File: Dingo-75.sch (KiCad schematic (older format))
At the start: 178 parts, among them SW1 SW_Push, U1 AT90USB1286-AU, Y1 16MHz

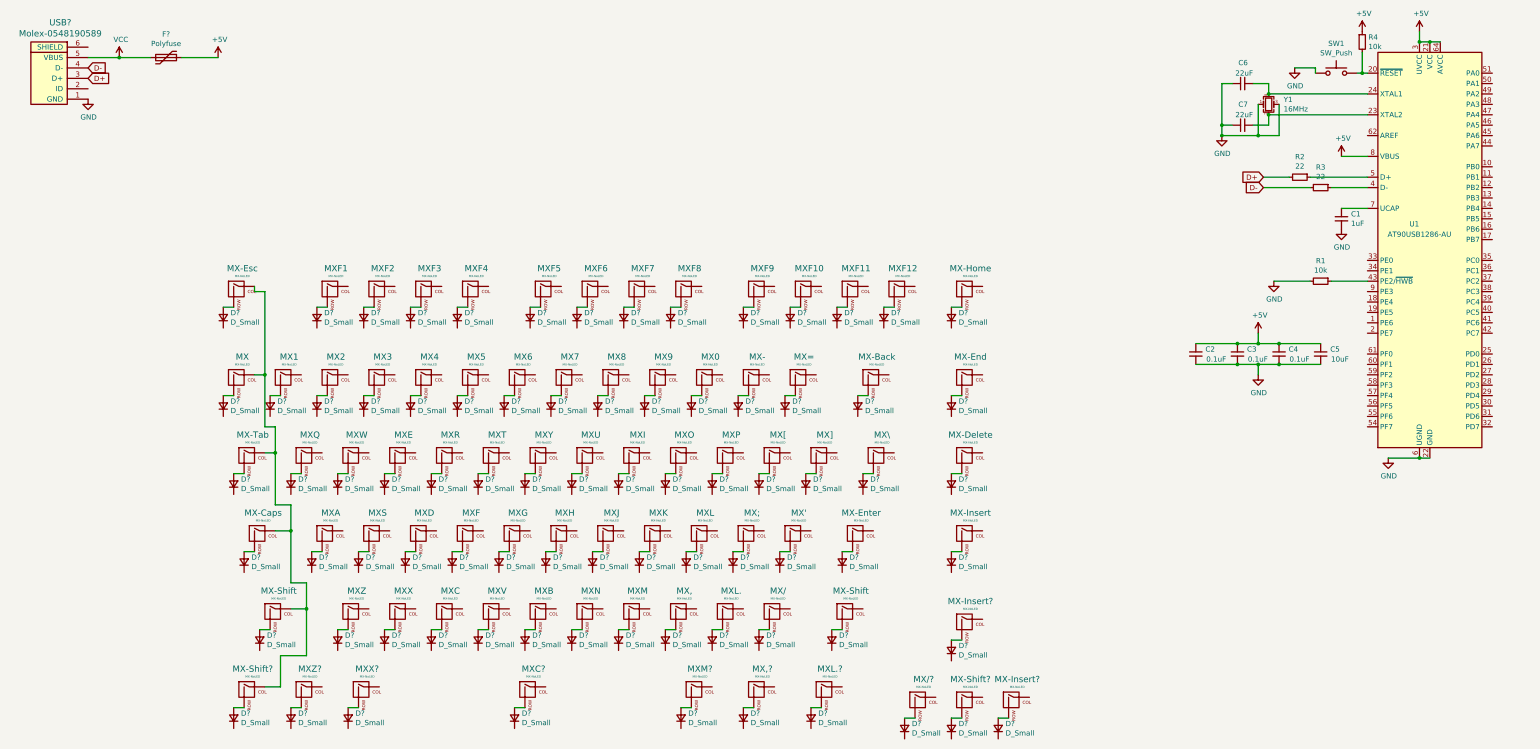
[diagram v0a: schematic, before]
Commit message: Completed switch matrix, started footprint assignment
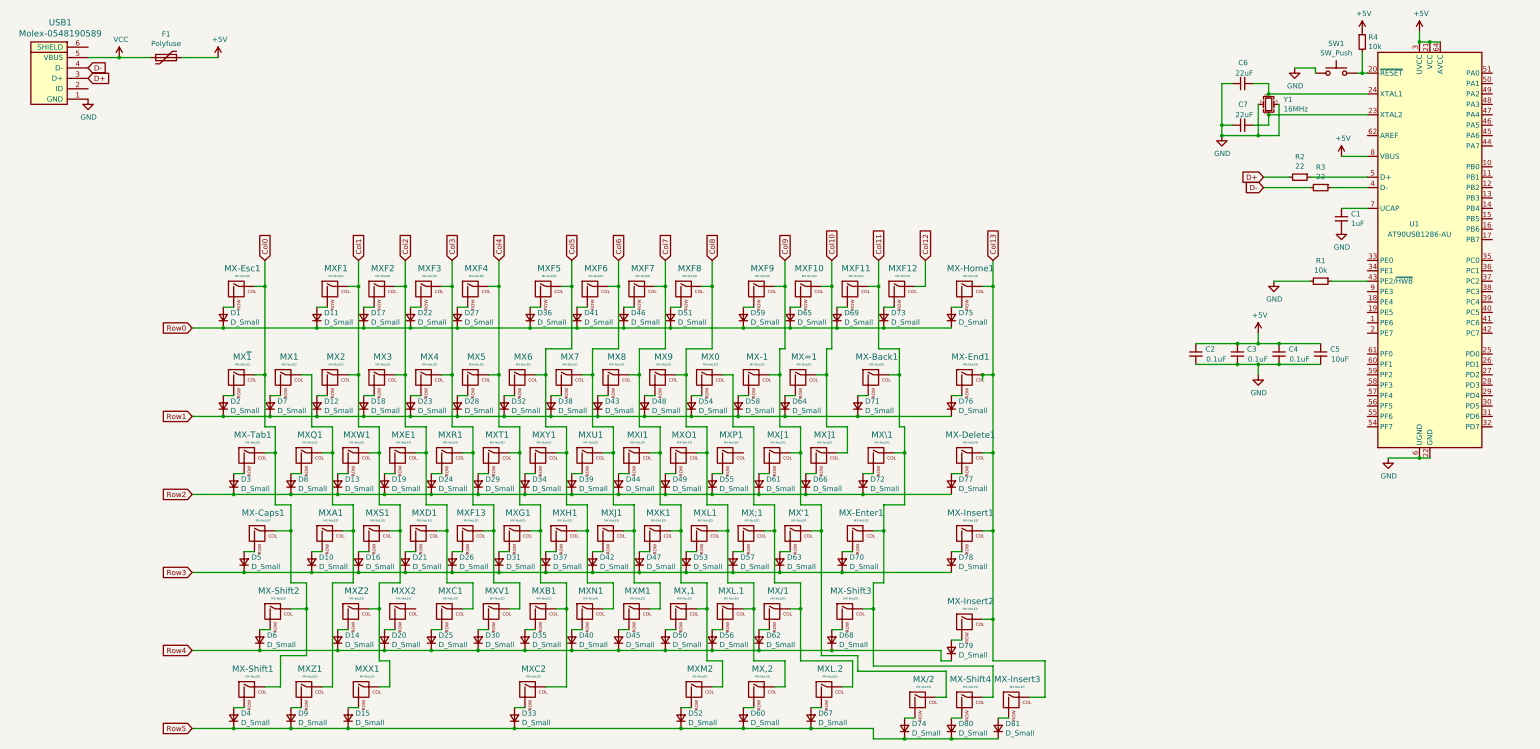
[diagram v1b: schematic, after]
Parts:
- C1, C2, C3, C4, C5, C6, C7: footprint (none) -> Capacitor_SMD:C_0805_2012Metric
- D1, D10, D11, D12, D13, D14, D15, D16, D17, D18, D19, D2, D20, D21, D22, D23, D24, D25, D26, D27, D28, D29, D3, D30, D31, D32, D33, D34, D35, D36, D37, D38, D39, D4, D40, D41, D42, D43, D44, D45, D46, D47, D48, D49, D5, D50, D51, D52, D53, D54, D55, D56, D57, D58, D59, D6, D60, D61, D62, D63, D64, D65, D66, D67, D68, D69, D7, D70, D71, D72, D73, D74, D75, D76, D77, D78, D79, D8, D80, D81, D9: renamed from D?; footprint (none) -> Diode_SMD:D_SOD-123
- F1: renamed from F?; footprint (none) -> Fuse:Fuse_1206_3216Metric
- MX'1: renamed from MX'; footprint (none) -> MX_Alps_Hybrid:MX-1U-NoLED
- MX,1: renamed from MX,; footprint (none) -> MX_Alps_Hybrid:MX-1U-NoLED
- MX,2: renamed from MX,?; footprint (none) -> MX_Alps_Hybrid:MX-1U-NoLED
- MX-1: renamed from MX-; footprint (none) -> MX_Alps_Hybrid:MX-1U-NoLED
- MX-Back1: renamed from MX-Back; footprint (none) -> MX_Alps_Hybrid:MX-1U-NoLED
- MX-Caps1: renamed from MX-Caps; footprint (none) -> MX_Alps_Hybrid:MX-1U-NoLED
- MX-Delete1: renamed from MX-Delete; footprint (none) -> MX_Alps_Hybrid:MX-1U-NoLED
- MX-End1: renamed from MX-End; footprint (none) -> MX_Alps_Hybrid:MX-1U-NoLED
- MX-Enter1: renamed from MX-Enter; footprint (none) -> MX_Alps_Hybrid:MX-1U-NoLED
- MX-Esc1: renamed from MX-Esc; footprint (none) -> MX_Alps_Hybrid:MX-1U-NoLED
- MX-Home1: renamed from MX-Home; footprint (none) -> MX_Alps_Hybrid:MX-1U-NoLED
- MX-Insert1: renamed from MX-Insert; footprint (none) -> MX_Alps_Hybrid:MX-1U-NoLED
- MX-Insert2, MX-Insert3: renamed from MX-Insert?; footprint (none) -> MX_Alps_Hybrid:MX-1U-NoLED
- MX-Shift1, MX-Shift4: renamed from MX-Shift?; footprint (none) -> MX_Alps_Hybrid:MX-1U-NoLED
- MX-Shift2, MX-Shift3: renamed from MX-Shift; footprint (none) -> MX_Alps_Hybrid:MX-1U-NoLED
- MX-Tab1: renamed from MX-Tab; footprint (none) -> MX_Alps_Hybrid:MX-1U-NoLED
- MX/1: renamed from MX/; footprint (none) -> MX_Alps_Hybrid:MX-1U-NoLED
- MX/2: renamed from MX/?; footprint (none) -> MX_Alps_Hybrid:MX-1U-NoLED
- MX0, MX1, MX2, MX3, MX4, MX5, MX6, MX7, MX8, MX9, MXF1, MXF10, MXF11, MXF12, MXF2, MXF3, MXF4, MXF5, MXF6, MXF7, MXF8, MXF9: footprint (none) -> MX_Alps_Hybrid:MX-1U-NoLED
- MX;1: renamed from MX;; footprint (none) -> MX_Alps_Hybrid:MX-1U-NoLED
- MX=1: renamed from MX=; footprint (none) -> MX_Alps_Hybrid:MX-1U-NoLED
- MXA1: renamed from MXA; footprint (none) -> MX_Alps_Hybrid:MX-1U-NoLED
- MXB1: renamed from MXB; footprint (none) -> MX_Alps_Hybrid:MX-1U-NoLED
- MXC1: renamed from MXC; footprint (none) -> MX_Alps_Hybrid:MX-1U-NoLED
- MXC2: renamed from MXC?; footprint (none) -> MX_Alps_Hybrid:MX-1U-NoLED
- MXD1: renamed from MXD; footprint (none) -> MX_Alps_Hybrid:MX-1U-NoLED
- MXE1: renamed from MXE; footprint (none) -> MX_Alps_Hybrid:MX-1U-NoLED
- MXF13: renamed from MXF; footprint (none) -> MX_Alps_Hybrid:MX-1U-NoLED
- MXG1: renamed from MXG; footprint (none) -> MX_Alps_Hybrid:MX-1U-NoLED
- MXH1: renamed from MXH; footprint (none) -> MX_Alps_Hybrid:MX-1U-NoLED
- MXI1: renamed from MXI; footprint (none) -> MX_Alps_Hybrid:MX-1U-NoLED
- MXJ1: renamed from MXJ; footprint (none) -> MX_Alps_Hybrid:MX-1U-NoLED
- MXK1: renamed from MXK; footprint (none) -> MX_Alps_Hybrid:MX-1U-NoLED
- MXL.1: renamed from MXL.; footprint (none) -> MX_Alps_Hybrid:MX-1U-NoLED
- MXL.2: renamed from MXL.?; footprint (none) -> MX_Alps_Hybrid:MX-1U-NoLED
- MXL1: renamed from MXL; footprint (none) -> MX_Alps_Hybrid:MX-1U-NoLED
- MXM1: renamed from MXM; footprint (none) -> MX_Alps_Hybrid:MX-1U-NoLED
- MXM2: renamed from MXM?; footprint (none) -> MX_Alps_Hybrid:MX-1U-NoLED
- MXN1: renamed from MXN; footprint (none) -> MX_Alps_Hybrid:MX-1U-NoLED
- MXO1: renamed from MXO; footprint (none) -> MX_Alps_Hybrid:MX-1U-NoLED
- MXP1: renamed from MXP; footprint (none) -> MX_Alps_Hybrid:MX-1U-NoLED
- MXQ1: renamed from MXQ; footprint (none) -> MX_Alps_Hybrid:MX-1U-NoLED
- MXR1: renamed from MXR; footprint (none) -> MX_Alps_Hybrid:MX-1U-NoLED
- MXS1: renamed from MXS; footprint (none) -> MX_Alps_Hybrid:MX-1U-NoLED
- MXT1: renamed from MXT; footprint (none) -> MX_Alps_Hybrid:MX-1U-NoLED
- MXU1: renamed from MXU; footprint (none) -> MX_Alps_Hybrid:MX-1U-NoLED
- MXV1: renamed from MXV; footprint (none) -> MX_Alps_Hybrid:MX-1U-NoLED
- MXW1: renamed from MXW; footprint (none) -> MX_Alps_Hybrid:MX-1U-NoLED
- MXX1: renamed from MXX?; footprint (none) -> MX_Alps_Hybrid:MX-1U-NoLED
- MXX2: renamed from MXX; footprint (none) -> MX_Alps_Hybrid:MX-1U-NoLED
- MXY1: renamed from MXY; footprint (none) -> MX_Alps_Hybrid:MX-1U-NoLED
- MXZ1: renamed from MXZ?; footprint (none) -> MX_Alps_Hybrid:MX-1U-NoLED
- MXZ2: renamed from MXZ; footprint (none) -> MX_Alps_Hybrid:MX-1U-NoLED
- MX[1: renamed from MX[; footprint (none) -> MX_Alps_Hybrid:MX-1U-NoLED
- MX\1: renamed from MX\; footprint (none) -> MX_Alps_Hybrid:MX-1U-NoLED
- MX]1: renamed from MX]; footprint (none) -> MX_Alps_Hybrid:MX-1U-NoLED
- MX~1: renamed from MX~; footprint (none) -> MX_Alps_Hybrid:MX-1U-NoLED
- R1, R2, R3, R4: footprint (none) -> Resistor_SMD:R_0805_2012Metric
- gave numbers to parts that had none: 1
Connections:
- net Col0: now reaches MX-Caps1.1 (COL), MX-Esc1.1 (COL), MX-Shift1.1 (COL), MX-Shift2.1 (COL), MX-Tab1.1 (COL), MX~1.1 (COL)
- net Row1: now reaches D2.1 (K)
- net Row1: now also D12.1 (K), D18.1 (K), D23.1 (K), D28.1 (K), D32.1 (K), D38.1 (K), D43.1 (K), D48.1 (K), D54.1 (K), D58.1 (K), D64.1 (K), D7.1 (K), D71.1 (K), D76.1 (K)
- net at MX1.1 (COL): now also MXA1.1 (COL), MXQ1.1 (COL), MXZ1.1 (COL)
- net Col1: now reaches MX2.1 (COL)
- net Col1: now also MXF1.1 (COL), MXS1.1 (COL), MXW1.1 (COL), MXX1.1 (COL), MXZ2.1 (COL)
- net Col2: now reaches MX3.1 (COL)
- net Col2: now also MXC1.1 (COL), MXD1.1 (COL), MXE1.1 (COL), MXF2.1 (COL)
- net Col3: now reaches MX4.1 (COL)
- net Col3: now also MXF13.1 (COL), MXF3.1 (COL), MXR1.1 (COL), MXV1.1 (COL)
- net Col4: now reaches MX5.1 (COL)
- net Col4: now also MXB1.1 (COL), MXC2.1 (COL), MXF4.1 (COL), MXG1.1 (COL), MXT1.1 (COL)
- net Col5: now reaches MX6.1 (COL)
- net Col5: now also MXF5.1 (COL), MXH1.1 (COL), MXN1.1 (COL), MXY1.1 (COL)
- net Col6: now reaches MX7.1 (COL)
- net Col6: now also MXF6.1 (COL), MXJ1.1 (COL), MXM1.1 (COL), MXU1.1 (COL)
- net Col7: now reaches MX8.1 (COL)
- net Col7: now also MX,1.1 (COL), MXF7.1 (COL), MXI1.1 (COL), MXK1.1 (COL), MXM2.1 (COL)
- net Col8: now reaches MX9.1 (COL)
- net Col8: now also MX,2.1 (COL), MXF8.1 (COL), MXL.1.1 (COL), MXL1.1 (COL), MXO1.1 (COL)
- net at MX0.1 (COL): now also MX/1.1 (COL), MX;1.1 (COL), MXL.2.1 (COL)
- net Col9: now reaches MX-1.1 (COL)
- net Col9: now also MX'1.1 (COL), MX/2.1 (COL), MXF9.1 (COL), MX[1.1 (COL)
- net Col10: now reaches MX=1.1 (COL)
- net Col10: now also MXF10.1 (COL), MX]1.1 (COL)
- net Col11: now reaches MX-Back1.1 (COL)
- net Col11: now also MX-Enter1.1 (COL), MX-Shift3.1 (COL), MX-Shift4.1 (COL), MXF11.1 (COL), MX\1.1 (COL)
- net Col13: now reaches MX-End1.1 (COL)
- net Col13: now also MX-Delete1.1 (COL), MX-Home1.1 (COL), MX-Insert1.1 (COL), MX-Insert2.1 (COL), MX-Insert3.1 (COL)
- net Row0: now reaches D1.1 (K)
- net Row0: now also D11.1 (K), D17.1 (K), D22.1 (K), D27.1 (K), D36.1 (K), D41.1 (K), D46.1 (K), D51.1 (K), D59.1 (K), D65.1 (K), D69.1 (K), D73.1 (K), D75.1 (K)
- net Col12: now reaches MXF12.1 (COL)
- net Row2: now reaches D3.1 (K)
- net Row2: now also D13.1 (K), D19.1 (K), D24.1 (K), D29.1 (K), D34.1 (K), D39.1 (K), D44.1 (K), D49.1 (K), D55.1 (K), D61.1 (K), D66.1 (K), D72.1 (K), D77.1 (K), D8.1 (K)
- net Row3: now reaches D5.1 (K)
- net Row3: now also D10.1 (K), D16.1 (K), D21.1 (K), D26.1 (K), D31.1 (K), D37.1 (K), D42.1 (K), D47.1 (K), D53.1 (K), D57.1 (K), D63.1 (K), D70.1 (K), D78.1 (K)
- net Row4: now reaches D6.1 (K)
- net Row4: now also D14.1 (K), D20.1 (K), D25.1 (K), D30.1 (K), D35.1 (K), D40.1 (K), D45.1 (K), D50.1 (K), D56.1 (K), D62.1 (K), D68.1 (K), D79.1 (K)
- net Row5: now reaches D4.1 (K)
- net Row5: now also D15.1 (K), D33.1 (K), D52.1 (K), D60.1 (K), D67.1 (K), D74.1 (K), D80.1 (K), D81.1 (K), D9.1 (K)

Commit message: Completed Footprint Assignment, Completed Board Layout, Started trace routing
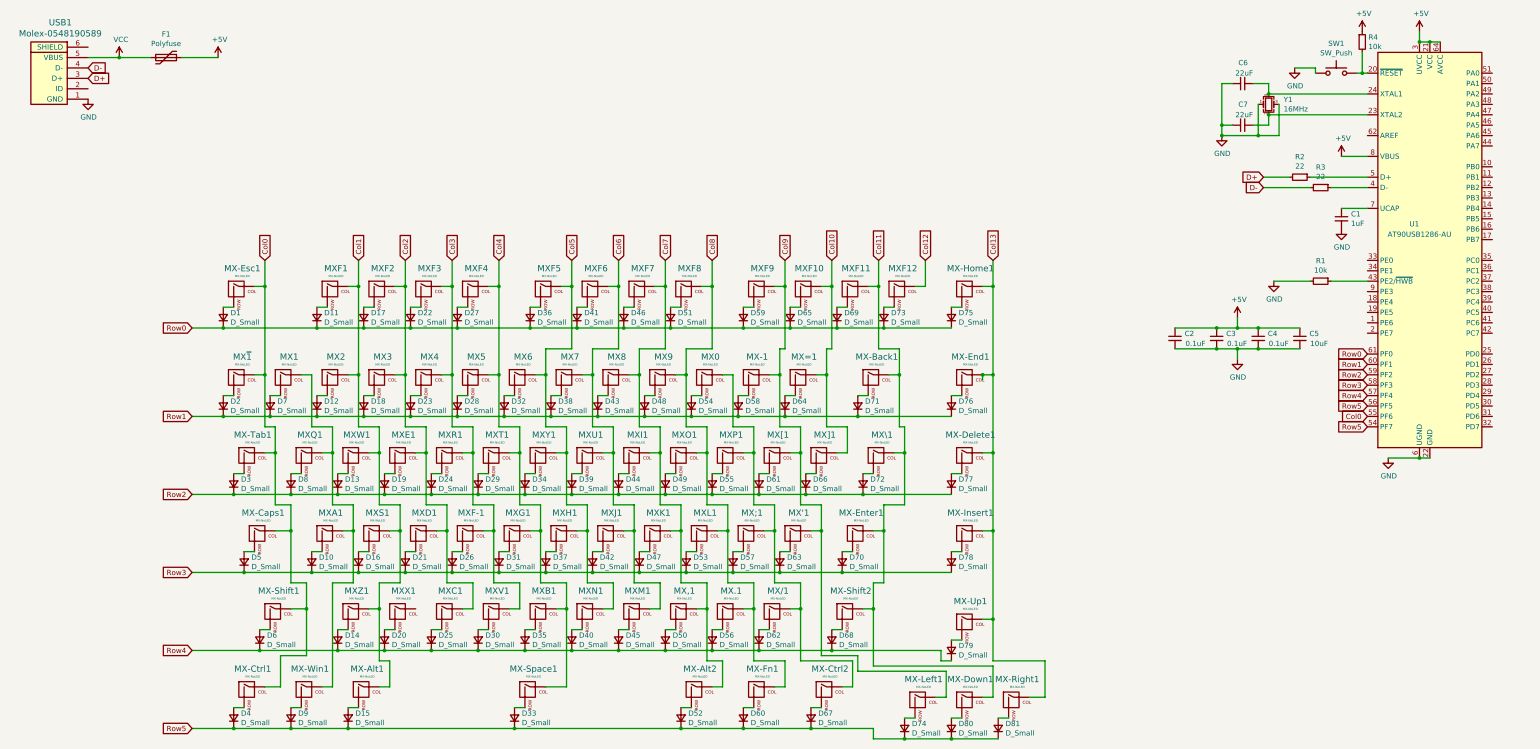
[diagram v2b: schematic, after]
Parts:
- SW1: footprint (none) -> random-keyboard-parts:SKQG-1155865
- USB1: footprint (none) -> random-keyboard-parts:Molex-0548190589
- Y1: footprint (none) -> Crystal:Crystal_SMD_3225-4Pin_3.2x2.5mm
- renumbered MXX1 to MX-Alt1, MXM2 to MX-Alt2, MX-Shift1 to MX-Ctrl1, MXL.2 to MX-Ctrl2, MX-Shift4 to MX-Down1, MX,2 to MX-Fn1, MX/2 to MX-Left1, MX-Insert3 to MX-Right1, MX-Shift2 to MX-Shift1, MX-Shift3 to MX-Shift2, MXC2 to MX-Space1, MX-Insert2 to MX-Up1, MXZ1 to MX-Win1, MXL.1 to MX.1, MXF13 to MXF-1, MXX2 to MXX1, MXZ2 to MXZ1
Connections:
- net Col0: now also U1.55 (PF6)
- net Row0: now also U1.61 (PF0)
- net Row1: now also U1.60 (PF1)
- net Row2: now also U1.59 (PF2)
- net Row3: now also U1.58 (PF3)
- net Row4: now also U1.57 (PF4)
- net Row5: now also U1.54 (PF7), U1.56 (PF5)
- net at MX-Ctrl2.1 (COL), MX/1.1 (COL), MX0.1 (COL)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: now also MXP1.1 (COL)
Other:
- moved on the sheet: C2, C3, C4, C5

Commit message: Completed routing
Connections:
- net Col0: now also U1.38 (PC3); no longer U1.55 (PF6)
- net Col1: now also MX-Win1.1 (COL), MX1.1 (COL), MXA1.1 (COL), MXQ1.1 (COL), U1.39 (PC4); no longer MX-Alt1.1 (COL), MX2.1 (COL), MXF1.1 (COL), MXS1.1 (COL), MXW1.1 (COL), MXZ1.1 (COL)
- net Col10: now also MX-Ctrl2.1 (COL), MX.1.1 (COL), MX0.1 (COL), MX;1.1 (COL), MXF9.1 (COL), MXP1.1 (COL), U1.49 (PA2); no longer MX=1.1 (COL), MXF10.1 (COL), MX]1.1 (COL)
- net Col11: now also MX'1.1 (COL), MX-1.1 (COL), MX-Left1.1 (COL), MX/1.1 (COL), MXF10.1 (COL), MX[1.1 (COL), U1.50 (PA1); no longer MX-Back1.1 (COL), MX-Down1.1 (COL), MX-Enter1.1 (COL), MX-Shift2.1 (COL), MXF11.1 (COL), MX\1.1 (COL)
- net Col12: now also MX=1.1 (COL), MXF11.1 (COL), MX]1.1 (COL), U1.51 (PA0); no longer MXF12.1 (COL)
- net Col13: now also MX-Back1.1 (COL), MX-Down1.1 (COL), MX-Enter1.1 (COL), MX-Shift2.1 (COL), MXF12.1 (COL), MX\1.1 (COL), U1.54 (PF7); no longer MX-Delete1.1 (COL), MX-End1.1 (COL), MX-Home1.1 (COL), MX-Insert1.1 (COL), MX-Right1.1 (COL), MX-Up1.1 (COL)
- net Col2: now also MX-Alt1.1 (COL), MX2.1 (COL), MXF1.1 (COL), MXS1.1 (COL), MXW1.1 (COL), MXZ1.1 (COL), U1.40 (PC5); no longer MX3.1 (COL), MXC1.1 (COL), MXD1.1 (COL), MXE1.1 (COL), MXF2.1 (COL)
- net Col3: now also MX3.1 (COL), MXD1.1 (COL), MXE1.1 (COL), MXF2.1 (COL), MXX1.1 (COL), U1.41 (PC6); no longer MX4.1 (COL), MXF-1.1 (COL), MXF3.1 (COL), MXR1.1 (COL), MXV1.1 (COL)
- net Col4: now also MX4.1 (COL), MXC1.1 (COL), MXF-1.1 (COL), MXF3.1 (COL), MXR1.1 (COL), U1.42 (PC7); no longer MX-Space1.1 (COL), MX5.1 (COL), MXB1.1 (COL), MXF4.1 (COL), MXG1.1 (COL), MXT1.1 (COL)
- net Col5: now also MX5.1 (COL), MXF4.1 (COL), MXG1.1 (COL), MXT1.1 (COL), MXV1.1 (COL), U1.44 (PA7); no longer MX6.1 (COL), MXF5.1 (COL), MXH1.1 (COL), MXN1.1 (COL), MXY1.1 (COL)
- net Col6: now also MX-Space1.1 (COL), MX6.1 (COL), MXB1.1 (COL), MXF5.1 (COL), MXH1.1 (COL), MXY1.1 (COL), U1.45 (PA6); no longer MX7.1 (COL), MXF6.1 (COL), MXJ1.1 (COL), MXM1.1 (COL), MXU1.1 (COL)
- net Col7: now also MX7.1 (COL), MXF6.1 (COL), MXJ1.1 (COL), MXN1.1 (COL), MXU1.1 (COL), U1.46 (PA5); no longer MX,1.1 (COL), MX-Alt2.1 (COL), MX8.1 (COL), MXF7.1 (COL), MXI1.1 (COL), MXK1.1 (COL)
- net Col8: now also MX-Alt2.1 (COL), MX8.1 (COL), MXF7.1 (COL), MXI1.1 (COL), MXK1.1 (COL), MXM1.1 (COL), U1.47 (PA4); no longer MX-Fn1.1 (COL), MX.1.1 (COL), MX9.1 (COL), MXF8.1 (COL), MXL1.1 (COL), MXO1.1 (COL)
- net Col9: now also MX,1.1 (COL), MX-Fn1.1 (COL), MX9.1 (COL), MXF8.1 (COL), MXL1.1 (COL), MXO1.1 (COL), U1.48 (PA3); no longer MX'1.1 (COL), MX-1.1 (COL), MX-Left1.1 (COL), MXF9.1 (COL), MX[1.1 (COL)
- net Row5: no longer U1.54 (PF7)
- new net Col14: MX-Delete1.1 (COL), MX-End1.1 (COL), MX-Home1.1 (COL), MX-Insert1.1 (COL), MX-Right1.1 (COL), MX-Up1.1 (COL), U1.55 (PF6)
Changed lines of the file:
@@
 	4900 5500 4900 5750
-Wire Wire Line
-	4900 6250 5150 6250
-Wire Wire Line
-	5150 6250 5150 6500
-Wire Wire Line
-	5150 6500 5050 6500
 Wire Wire Line
 	4800 5750 4900 5750
@@
 	5350 5500 5350 5750
 Wire Wire Line
-	5350 6250 5600 6250
-Wire Wire Line
 	5600 6250 5600 6500
 Wire Wire Line
@@
 	5800 5500 5800 5750
 Wire Wire Line
-	5800 6250 6050 6250
-Wire Wire Line
 	6050 6250 6050 6500
 Wire Wire Line
@@
 	6250 5500 6250 5750
 Wire Wire Line
-	6250 6250 6500 6250
-Wire Wire Line
 	6500 6250 6500 6500
 Wire Wire Line
@@
 	6700 5500 6700 5750
 Wire Wire Line
-	6700 6250 6950 6250
-Wire Wire Line
 	6950 6250 6950 6500
 Wire Wire Line
@@
 	7150 5500 7150 5750
 Wire Wire Line
-	7150 6250 7400 6250
-Wire Wire Line
 	7400 6250 7400 6500
 Wire Wire Line
@@
 	7600 5500 7600 5750
 Wire Wire Line
-	7600 6250 7850 6250
-Wire Wire Line
 	7850 6250 7850 6500
 Wire Wire Line
@@
 	8050 5500 8050 5750
 Wire Wire Line
-	8050 6250 8300 6250
-Wire Wire Line
 	8300 6250 8300 6500
 Wire Wire Line
@@
 	7850 4750 7850 5000
 Wire Wire Line
-	7400 6500 7400 7000
-Wire Wire Line
-	7400 7000 7550 7000
-Wire Wire Line
 	7550 7000 7550 7250
 Wire Wire Line
 	7550 7250 7450 7250
-Connection ~ 7400 6500
-Wire Wire Line
-	7850 6500 7850 7000
-Wire Wire Line
-	7850 7000 8150 7000
 Wire Wire Line
 	8150 7000 8150 7250
 Wire Wire Line
 	8150 7250 8050 7250
-Connection ~ 7850 6500
-Wire Wire Line
-	8300 6500 8300 7000
 Wire Wire Line
 	8300 7000 8800 7000
@@
 Wire Wire Line
 	8800 7250 8700 7250
-Connection ~ 8300 6500
 Wire Wire Line
 	8050 3400 8150 3400
 Wire Wire Line
-	8150 3400 8150 4000
-Wire Wire Line
-	8150 4000 8100 4000
-Wire Wire Line
 	8100 4000 8100 4250
 Wire Wire Line
@@
 	8500 3400 8600 3400
 Wire Wire Line
-	8600 3400 8600 4000
-Wire Wire Line
-	8600 4000 8550 4000
-Wire Wire Line
 	8550 4750 8750 4750
 Wire Wire Line
@@
 	8550 4000 8550 4250
 Wire Wire Line
-	8500 5750 8500 6950
+	8500 5750 8500 6250
 Wire Wire Line
 	8500 6950 8850 6950
@@
 	8950 3400 9050 3400
 Wire Wire Line
-	9050 3400 9050 4000
-Wire Wire Line
-	9050 4000 9250 4000
-Wire Wire Line
 	9250 4000 9250 4250
 Wire Wire Line
@@
 Wire Wire Line
 	9050 3400 9050 3150
-Connection ~ 9050 3400
 Wire Wire Line
 	8600 3400 8600 3150
-Connection ~ 8600 3400
 Wire Wire Line
 	8150 3400 8150 3150
-Connection ~ 8150 3400
 Wire Wire Line
 	7450 3400 7450 3150
@@
 	4300 6900 3850 6900
 Connection ~ 4750 6900
-Wire Wire Line
-	4750 6900 4300 6900
 Connection ~ 5200 6900
 Wire Wire Line
@@
 Text GLabel 3150 3150 1    50   Input ~ 0
 Col0
+Text GLabel 3600 3150 1    50   Input ~ 0
+Col1
 Text GLabel 4050 3150 1    50   Input ~ 0
-Col1
+Col2
 Text GLabel 4500 3150 1    50   Input ~ 0
-Col2
+Col3
 Text GLabel 4950 3150 1    50   Input ~ 0
-Col3
+Col4
 Text GLabel 5400 3150 1    50   Input ~ 0
-Col4
+Col5
 Text GLabel 6100 3150 1    50   Input ~ 0
-Col5
+Col6
 Text GLabel 6550 3150 1    50   Input ~ 0
-Col6
+Col7
 Text GLabel 7000 3150 1    50   Input ~ 0
-Col7
+Col8
 Text GLabel 7450 3150 1    50   Input ~ 0
-Col8
+Col9
 Text GLabel 8150 3150 1    50   Input ~ 0
-Col9
+Col10
 Text GLabel 8600 3150 1    50   Input ~ 0
-Col10
+Col11
 Text GLabel 9050 3150 1    50   Input ~ 0
-Col11
+Col12
 Text GLabel 9500 3150 1    50   Input ~ 0
-Col12
-Text GLabel 10150 3150 1    50   Input ~ 0
 Col13
 Text GLabel 2450 3800 0    50   Input ~ 0
@@
 Text GLabel 13750 4550 0    50   Input ~ 0
 Row5
+Text GLabel 13750 4750 0    50   Input ~ 0
+Col13
+Text GLabel 14950 1350 2    50   Input ~ 0
+Col12
+Wire Wire Line
+	4900 6250 4700 6250
+Wire Wire Line
+	4700 6250 4700 6500
+Wire Wire Line
+	4700 6500 4600 6500
+Wire Wire Line
+	5350 6250 5150 6250
+Wire Wire Line
+	5150 6250 5150 6500
+Wire Wire Line
+	5150 6500 5050 6500
+Wire Wire Line
+	4300 6900 4750 6900
+Wire Wire Line
+	5800 6250 5600 6250
+Wire Wire Line
+	6250 6250 6050 6250
+Wire Wire Line
+	6700 6250 6500 6250
+Wire Wire Line
+	8050 6250 7850 6250
+Wire Wire Line
+	7400 6250 7600 6250
+Wire Wire Line
+	8300 6250 8500 6250
+Connection ~ 8500 6250
+Wire Wire Line
+	8500 6250 8500 6950
+Wire Wire Line
+	7850 6500 7850 6950
+Wire Wire Line
+	7850 6950 8300 6950
+Wire Wire Line
+	8300 6950 8300 7000
+Connection ~ 7850 6500
+Wire Wire Line
+	7400 6500 7400 6950
+Wire Wire Line
+	7400 6950 7700 6950
+Wire Wire Line
+	7700 6950 7700 7000
+Wire Wire Line
+	7700 7000 8150 7000
+Connection ~ 7400 6500
+Wire Wire Line
+	6950 6500 6950 7000
+Wire Wire Line
+	6950 7000 7550 7000
+Connection ~ 6950 6500
+Wire Wire Line
+	6950 6250 7150 6250
+Text GLabel 14950 1450 2    50   Input ~ 0
+Col11
+Text GLabel 14950 1550 2    50   Input ~ 0
+Col10
+Text GLabel 14950 1650 2    50   Input ~ 0
+Col9
+Text GLabel 14950 1750 2    50   Input ~ 0
+Col8
+Text GLabel 14950 1850 2    50   Input ~ 0
+Col7
+Text GLabel 14950 1950 2    50   Input ~ 0
+Col6
+Text GLabel 14950 2050 2    50   Input ~ 0
+Col5
+Text GLabel 14950 3850 2    50   Input ~ 0
+Col4
+Wire Wire Line
+	8150 3400 8150 3900
+Wire Wire Line
+	8150 3900 7650 3900
+Wire Wire Line
+	7650 3900 7650 4250
+Connection ~ 8150 3400
+Connection ~ 7650 4250
+Wire Wire Line
+	8600 3400 8600 3900
+Wire Wire Line
+	8600 3900 8350 3900
+Wire Wire Line
+	8350 3900 8350 4000
+Wire Wire Line
+	8350 4000 8100 4000
+Connection ~ 8600 3400
+Wire Wire Line
+	9050 3400 9050 3900
+Wire Wire Line
+	9050 3900 8800 3900
+Wire Wire Line
+	8800 3900 8800 4000
+Wire Wire Line
+	8800 4000 8550 4000
+Connection ~ 9050 3400
+Wire Wire Line
+	9500 3400 9500 4000
+Wire Wire Line
+	9500 4000 9250 4000
+Connection ~ 9500 3400
+Wire Wire Line
+	3600 4250 3600 3150
+Connection ~ 3600 4250
+Text GLabel 10150 3150 1    50   Input ~ 0
+Col14
 Text GLabel 13750 4650 0    50   Input ~ 0
+Col14
+Text GLabel 14950 3750 2    50   Input ~ 0
+Col3
+Text GLabel 14950 3650 2    50   Input ~ 0
+Col2
+Text GLabel 14950 3550 2    50   Input ~ 0
+Col1
+Text GLabel 14950 3450 2    50   Input ~ 0
 Col0
-Text GLabel 13750 4750 0    50   Input ~ 0
-Row5
 $EndSCHEMATC
